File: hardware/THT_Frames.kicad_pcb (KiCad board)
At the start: 2 copper layers, 183.8 x 99.7 mm, 144 parts, among them J1 FRAME_IN, J10 1_OUT, J11 2_OUT, J12 3_OUT, J13 4_OUT, J14 POWER, J15 OFFSET_JUMPER, J16 ALL_IN, J17 MIX_OUT, J18 Conn_01x12_Male, J19 Conn_01x12_Female, J2 Serial, J20 Conn_01x12_Female, J21 Conn_01x12_Male, J22 Conn_01x12_Female, J3 Conn_01x12_Male, J5 STEP_OUT, J6 1_IN, J7 2_IN, J8 3_IN, J9 4_IN, Q1 2N3904, SW1 ADD, SW2 DEL, SW3 OFFSET, U1 TL072, U12 V2164, U13 TL072, U2 bluepill, U3 LM1117-3.3, U4 LM4040AIZ-10, U5 TL072, U6 MCP4822, U7 MCP4822, U8 TL074, U9 TL074

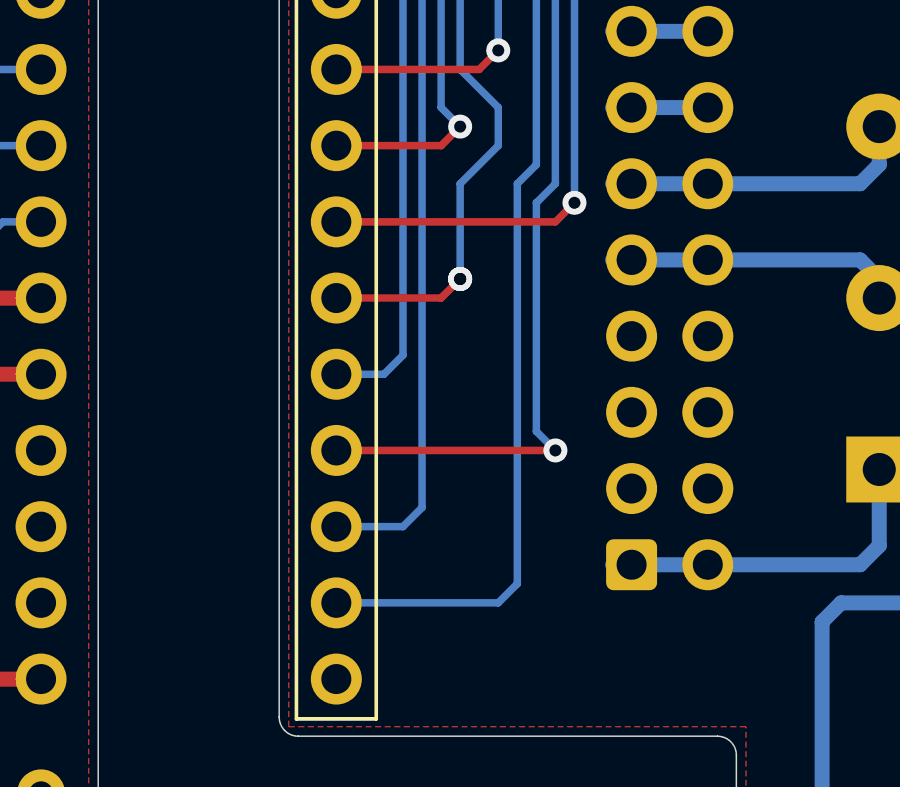
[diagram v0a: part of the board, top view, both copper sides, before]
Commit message: Fix swapped leds on channels 3/4
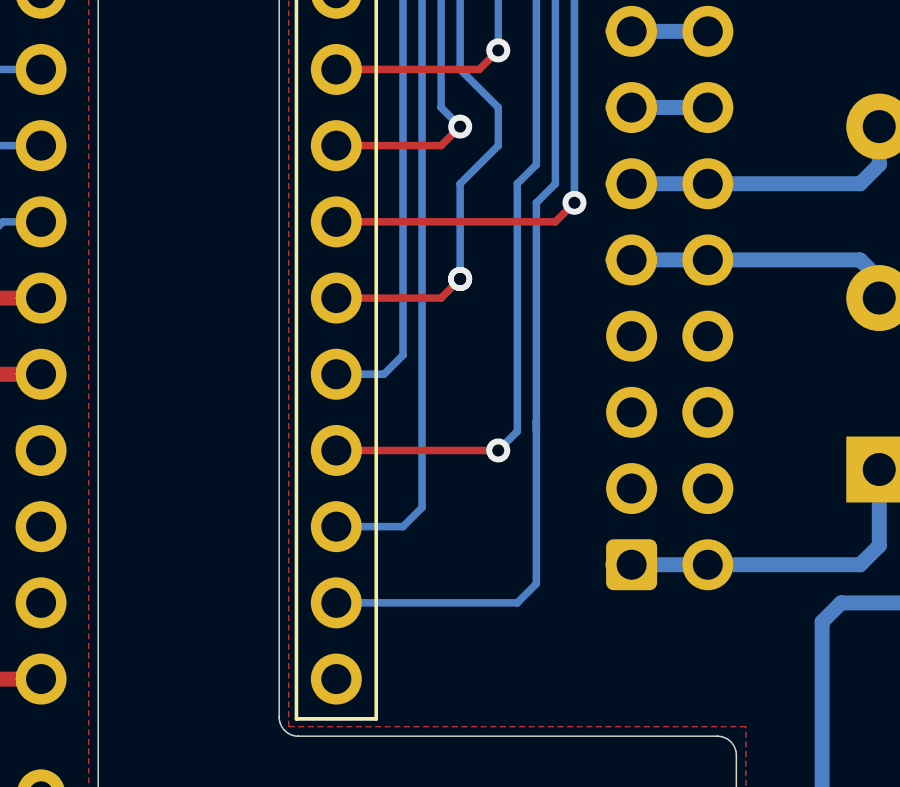
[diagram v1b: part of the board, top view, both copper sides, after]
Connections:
- J3 pad 11: /LED_CH3 -> /LED_CH4
- J3 pad 9: /LED_CH4 -> /LED_CH3
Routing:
- net /LED_CH3: track 70.5 -> 65.4 mm, vias 0 -> 1
- net /LED_CH4: track 69.2 -> 73.3 mm, vias 1 -> 0

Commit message: Use easy to solder to-92 footprint, bigger footprints for 1uF caps
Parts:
- C24, C25, C28, C29: footprint custom:C_Disc_D5.0mm_W2.5mm_P5.00mm_silk -> custom:C_Disc_D7.5mm_W5.0mm_P5.00mm_silk
- Q1, U4: footprint custom:TO-92_Inline_silk -> custom:TO-92_Inline_Wide_silk
- moved C28 11.7 mm to (142.9, -56.5)
- moved R55 10.2 mm to (148.6, -71.8)
- moved R56 10.2 mm to (148.6, -68.6)
- moved R54 7.96 mm to (144.1, -71.8), turned to 180 degrees
- moved C25 4.84 mm to (149.9, -56.5), turned to 0 degrees
- moved C29 4.84 mm to (149.9, -63.5), turned to 0 degrees
- moved R53 3.86 mm to (144.1, -68.6), turned to 180 degrees
- moved C24 2.84 mm to (142.9, -63.5)
- moved J2 2.54 mm to (145.4, -76.2)
- moved Q1 1.27 mm to (85.7, -38.7)
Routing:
- net Net-(R53-Pad2): track 12.6 -> 34.8 mm
- net Net-(R54-Pad2): track 10.7 -> 31.3 mm
- net /GAIN_4: track 42.7 -> 58.8 mm
- net /GAIN_3: track 33.1 -> 46.6 mm
- net /GAIN_2: track 35.0 -> 45.3 mm
- net Net-(R56-Pad2): track 7.77 -> 17.7 mm
- net Net-(R55-Pad2): track 6.99 -> 15.8 mm
- net /RX: track 13.9 -> 11.3 mm
- net Net-(J5-PadT): track 37.5 -> 36.2 mm
- net /LED_FRAME: track 63.2 -> 62.1 mm
- net /TX: track 13.9 -> 13.3 mm
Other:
- board text added: "tht frames by 30350n Rev.1"

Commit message: Add silkscreen markings to offset jumper
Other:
- board text added: "+10V"
- board text added: "+5V"
- board text added: "offset"

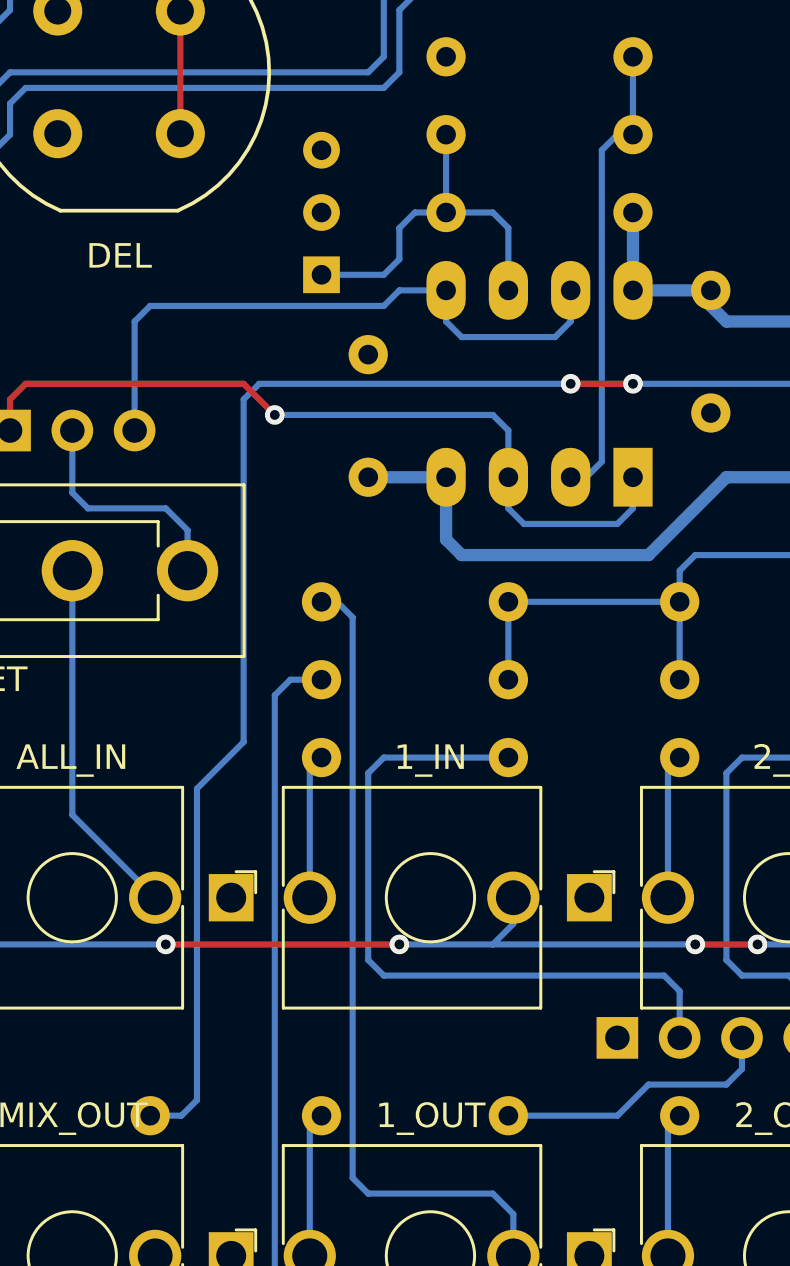
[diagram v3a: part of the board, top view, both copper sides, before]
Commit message: Fix accidentally inverted internal offset voltages
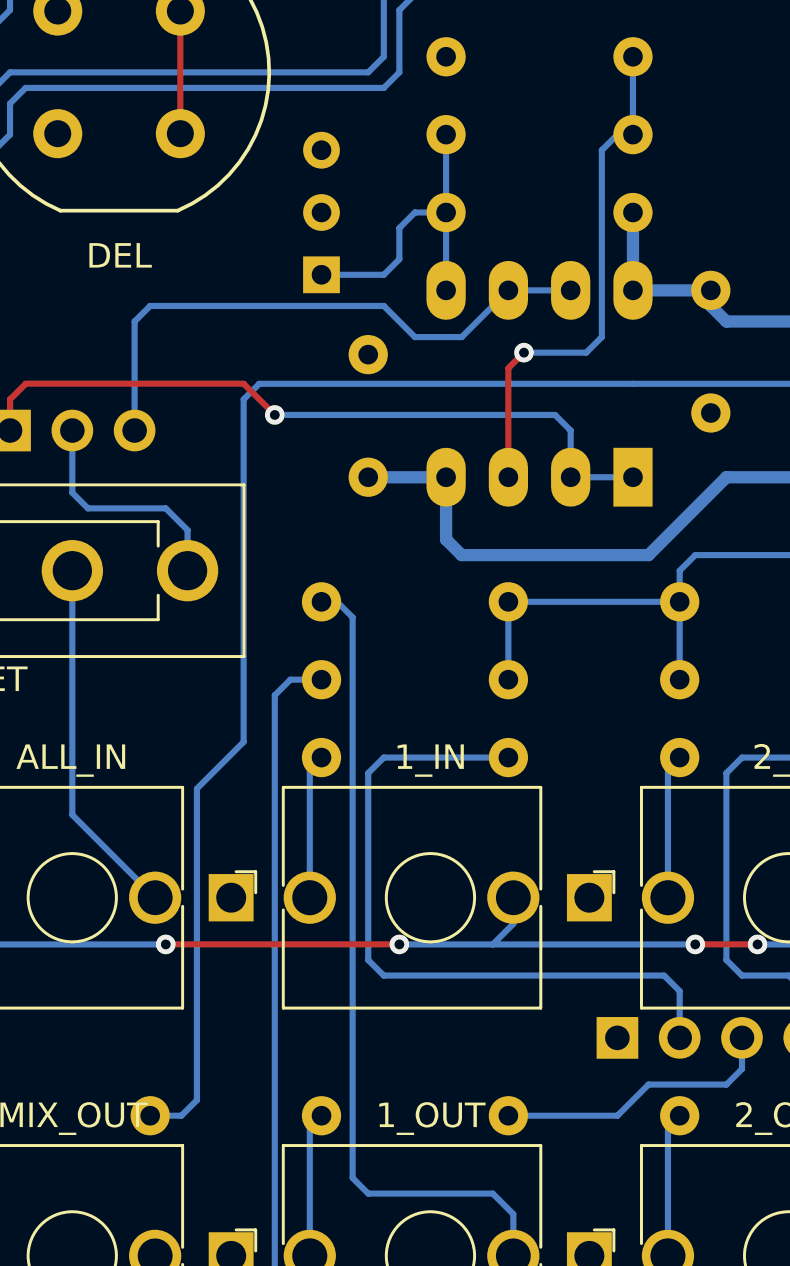
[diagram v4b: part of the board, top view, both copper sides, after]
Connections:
- U5 pad 2: Net-(R19-Pad2) -> /AREF_5
- U5 pad 3: /AREF_5 -> Net-(R19-Pad2)
- U5 pad 5: /AREF_10 -> Net-(R18-Pad2)
- U5 pad 6: Net-(R18-Pad2) -> /AREF_10
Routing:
- net /AREF_5: track 32.7 -> 30.3 mm
- net Net-(R19-Pad2): track 18.9 -> 21.1 mm, vias 0 -> 1
- net Net-(R18-Pad2): track 15.4 -> 13.2 mm
- net /AREF_10: track 25.8 -> 23.8 mm
- net Net-(C17-Pad1): vias 3 -> 1

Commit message: Bump revision number on main pcb
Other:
- board text removed: "tht frames by 30350n Rev.0"
